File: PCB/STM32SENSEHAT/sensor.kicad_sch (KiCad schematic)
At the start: 8 parts, among them U4 BME280, U5 TMP112xxDRL, U6 CAT24C256

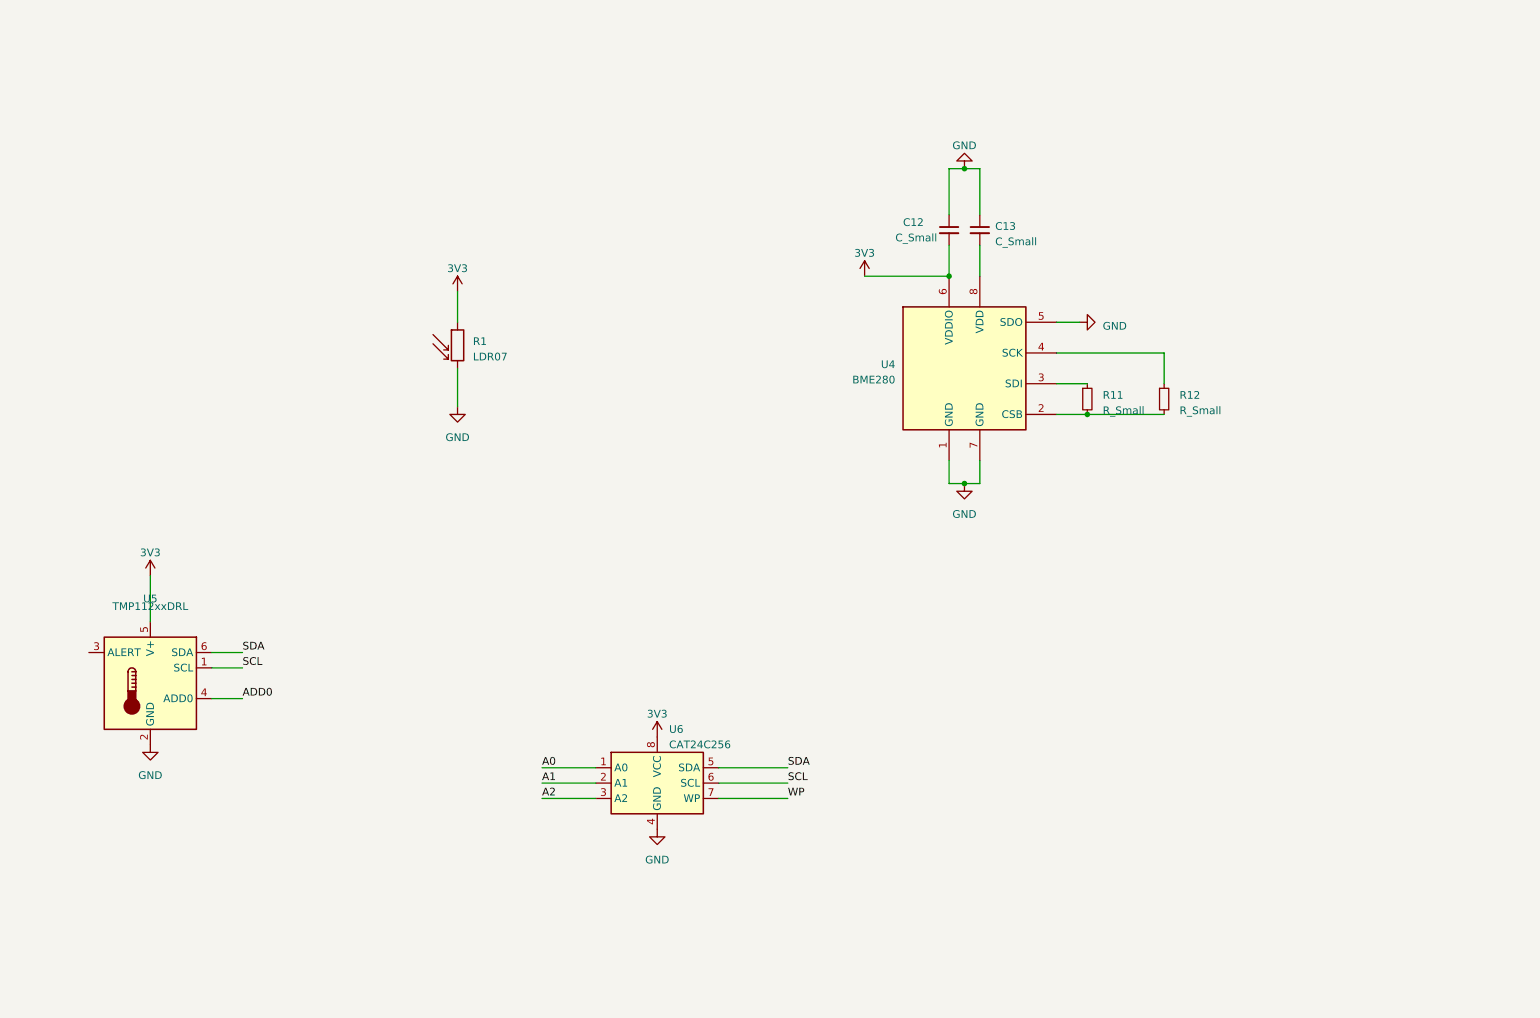
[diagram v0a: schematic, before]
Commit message: rework of top level sheet, MCU, power and sensor sheet
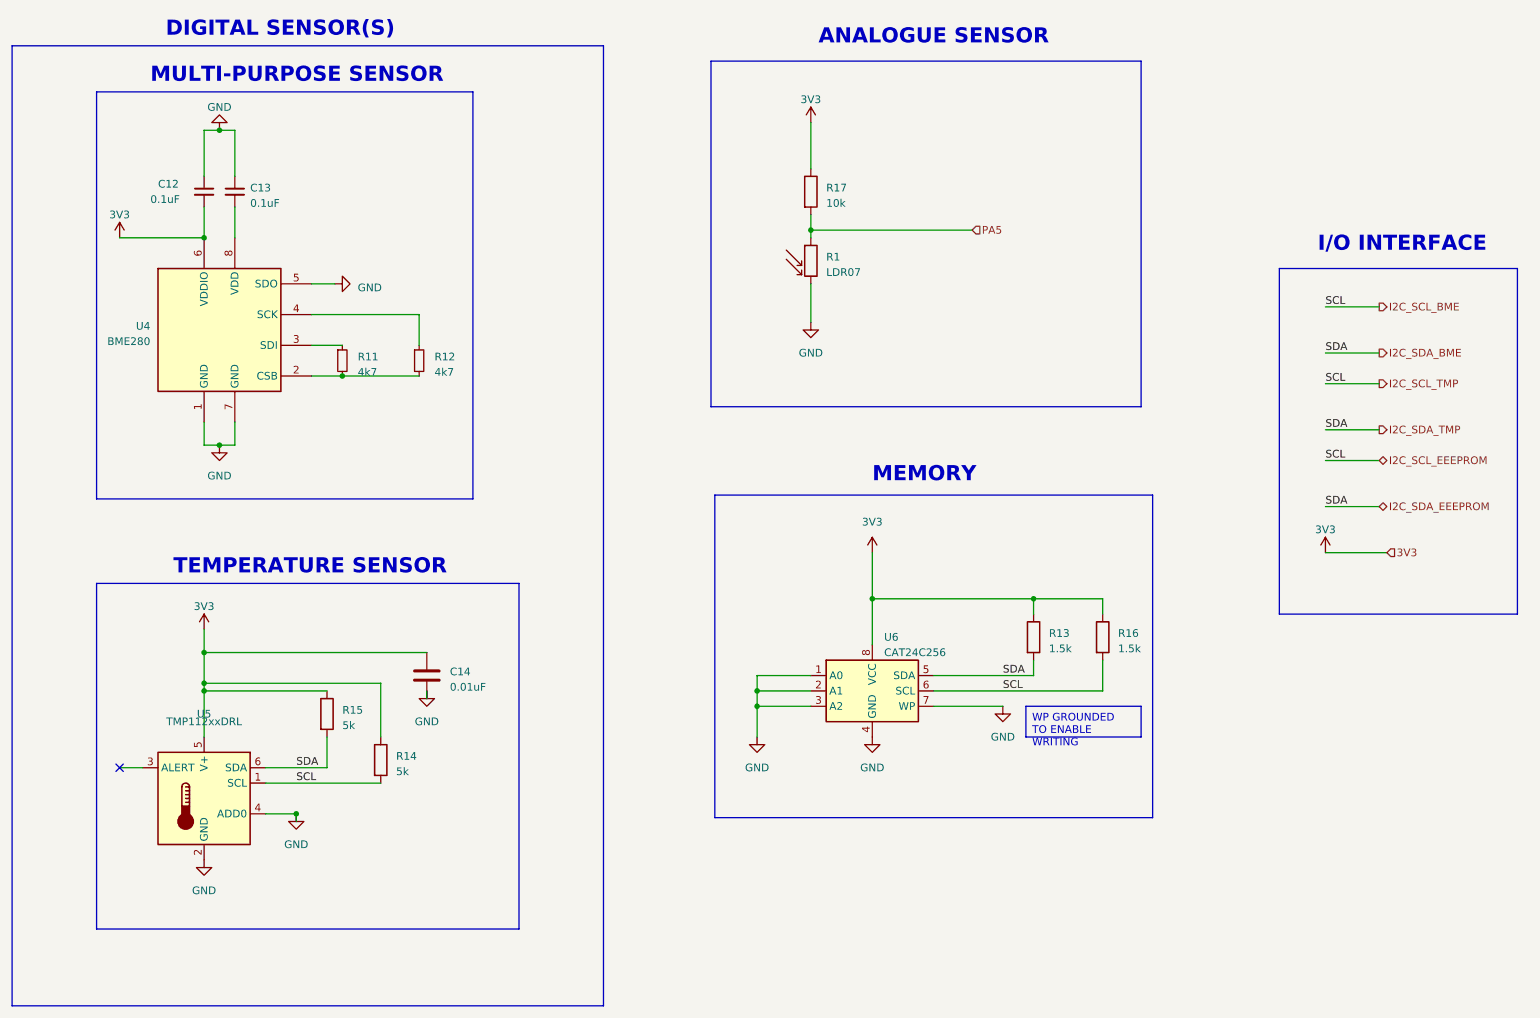
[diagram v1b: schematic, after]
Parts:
- added C14: 0.01uF, symbol Device:C
- added R13, R16: 1.5k, symbol Device:R
- added R14, R15: 5k, symbol Device:R
- added R17: 10k, symbol Device:R
- C12, C13: value C_Small -> 0.1uF
- R11, R12: value R_Small -> 4k7
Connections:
- net A0 is gone; now on net GND: U6.1 (A0)
- net A1 is gone; now on net GND: U6.2 (A1)
- net A2 is gone; now on net GND: U6.3 (A2)
- net ADD0 is gone; now on net GND: U5.4 (ADD0)
- net WP is gone; now on net GND: U6.7 (WP)
- net GND: now also C14.2
- net VCC: now also C14.1, R13.1, R14.1, R15.1, R16.1, R17.1; no longer R1.1
- net SCL renamed I2C_SCL_BME
- net I2C_SCL_BME: now also R14.2, R16.2
- net SDA renamed I2C_SDA_BME
- net I2C_SDA_BME: now also R13.2, R15.2
- new net PA5: R1.1, R17.2
- no-connect marks 0 -> 1
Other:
- note added: "ANALOGUE SENSOR"
- note added: "DIGITAL SENSOR(S)"
- note added: "I/O INTERFACE"
- note added: "MEMORY"
- note added: "MULTI-PURPOSE SENSOR"
- note added: "TEMPERATURE SENSOR"
- company: (none) -> IMPERIUM
- title: (none) -> SENSOR MODULE
- moved on the sheet: C12, C13, R1, R11, R12, U4, U5, U6
